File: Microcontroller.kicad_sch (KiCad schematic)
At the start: 9 parts, among them J1 GT-USB-7010ASV, SW1 CK_KMS2xxGP, U1 ESP32-S3-MINI-1

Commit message: Added power latch circuit.
Signed-off-by: James Mendel <jrm.mendel@gmail.com>
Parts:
- removed C7: 0.1u, symbol Device:C
- removed SW1: CK_KMS2xxGP, Button_Switch_SMD:SW_SPST_CK_KMS2xxGP, symbol Switch:CK_KMS2xxGP
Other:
- note removed: "Switch"

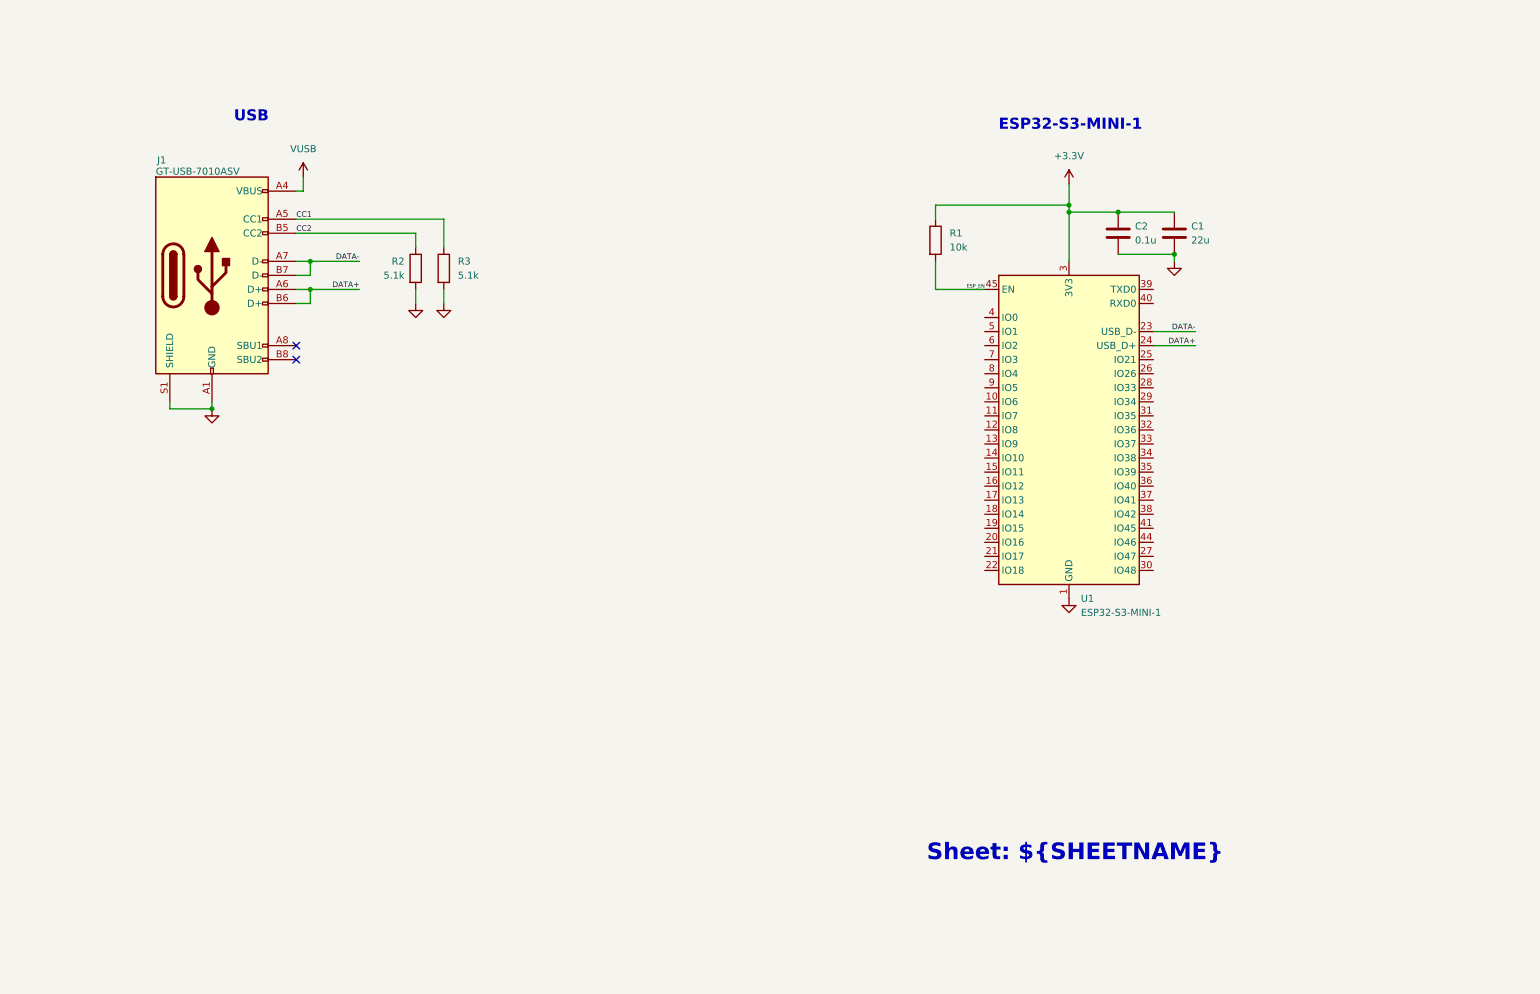
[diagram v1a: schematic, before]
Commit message: SCH and PCB updates. Added Integrated GPS and other features.
Signed-off-by: James Mendel <jrm.mendel@gmail.com>
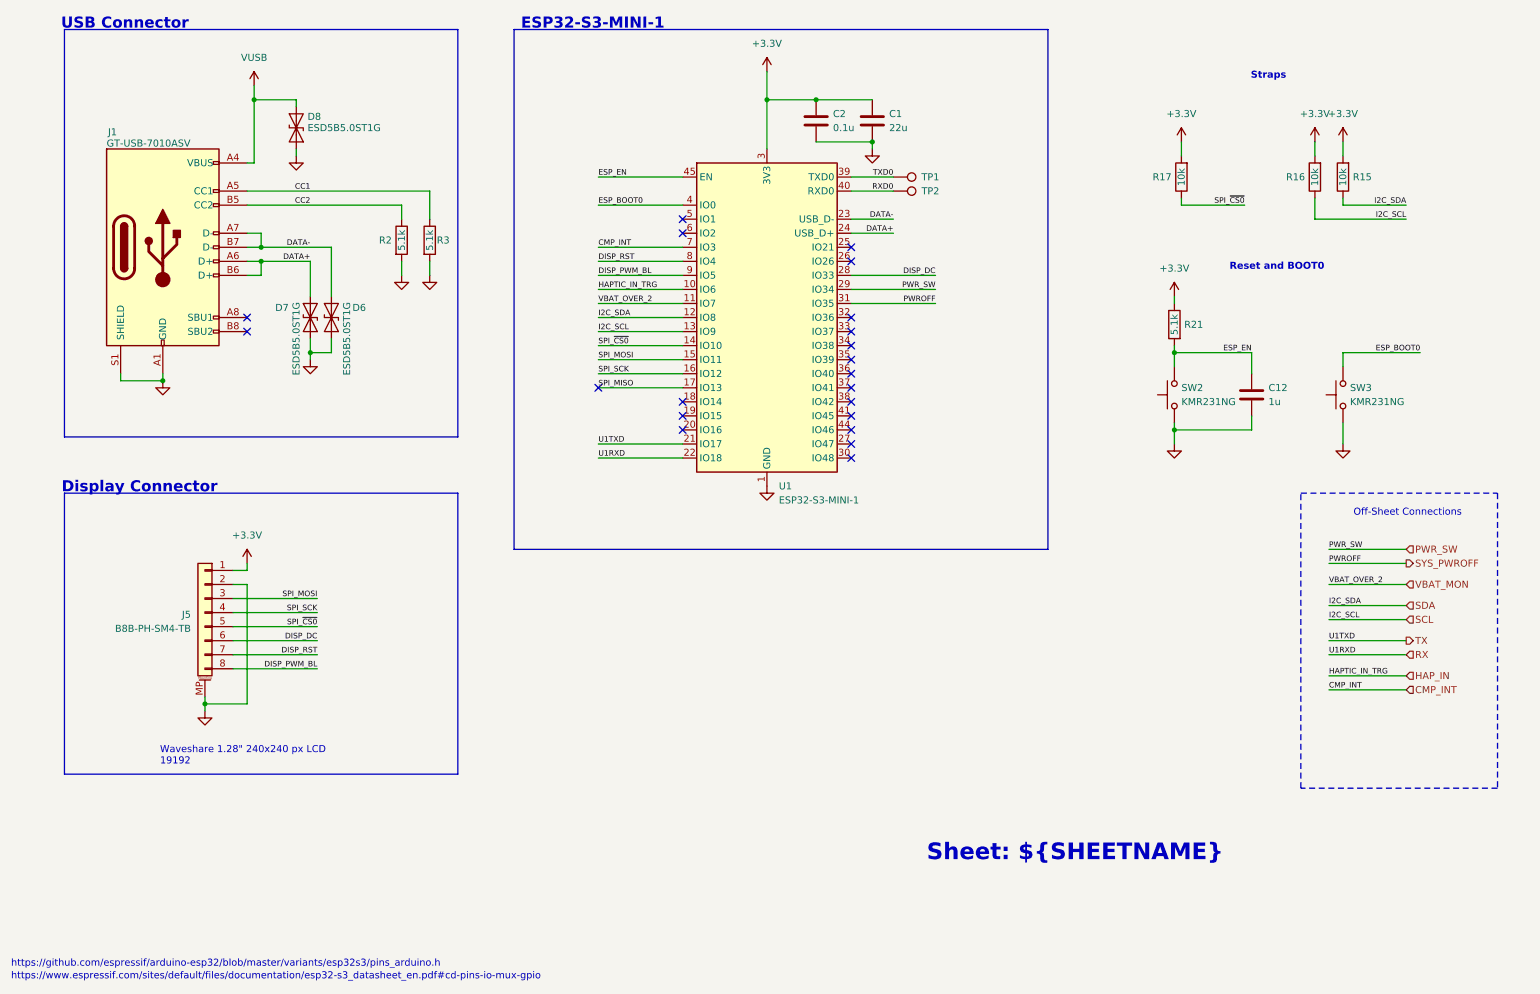
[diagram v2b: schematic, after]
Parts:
- removed R1: 10k, symbol Device:R
- added C12: 1u, Capacitor_SMD:C_0603_1608Metric, symbol Device:C
- added D6, D7, D8: ESD5B5.0ST1G, Diode_SMD:D_SOD-523, symbol Diode:ESD9B5.0ST5G
- added J5: B8B-PH-SM4-TB, Connector_JST:JST_PH_B8B-PH-SM4-TB_1x08-1MP_P2.00mm_Vertical, symbol Connector_Generic_MountingPin:Conn_01x08_MountingPin
- added R15, R16, R17: 10k, Resistor_SMD:R_0603_1608Metric, symbol Device:R
- added R21: 5.1k, Resistor_SMD:R_0603_1608Metric, symbol Device:R
- added SW2, SW3: KMR231NG, Button_Switch_SMD:SW_Push_1P1T_NO_CK_KMR2, symbol Switch:SW_Push
- added TP1: TXD0, TestPoint:TestPoint_Pad_D1.5mm, symbol Connector:TestPoint
- added TP2: RXD0, TestPoint:TestPoint_Pad_D1.5mm, symbol Connector:TestPoint
- C1, C2: footprint (none) -> Capacitor_SMD:C_0603_1608Metric
- J1: Alt1 (none) -> USB4105-GF-A; MPN (none) -> GT-USB-7010ASV
- R2, R3: footprint (none) -> Resistor_SMD:R_0603_1608Metric
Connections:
- net +3.3V: now also J5.1 (Pin_1), R15.2, R16.2, R17.2, R21.1
- net DATA+: now also D7.2 (A2)
- net DATA-: now also D6.2 (A2)
- net ESP_EN: now also C12.1, R21.2, SW2.2
- net GND: now also C12.2, D6.1 (A1), D7.1 (A1), D8.1 (A1), J5.2 (Pin_2), J5.MP (MountPin), SW2.1, SW3.1
- net VUSB: now also D8.2 (A2)
- net HAP_IN: now reaches U1.10 (IO6)
- net VBAT_MON: now reaches U1.11 (IO7)
- net SDA: now reaches U1.12 (IO8)
- net SDA: now also R15.1
- net SCL: now reaches U1.13 (IO9)
- net SCL: now also R16.1
- net SPI_~{CS0}: now reaches U1.14 (IO10)
- net SPI_~{CS0}: now also J5.5 (Pin_5), R17.1
- net SPI_MOSI: now reaches U1.15 (IO11)
- net SPI_MOSI: now also J5.3 (Pin_3)
- net SPI_SCK: now reaches U1.16 (IO12)
- net SPI_SCK: now also J5.4 (Pin_4)
- net SPI_MISO: now reaches U1.17 (IO13)
- net TX: now reaches U1.21 (IO17)
- net RX: now reaches U1.22 (IO18)
- net DISP_DC: now reaches U1.28 (IO33)
- net DISP_DC: now also J5.6 (Pin_6)
- net PWR_SW: now reaches U1.29 (IO34)
- net SYS_PWROFF: now reaches U1.31 (IO35)
- net TXD0: now reaches U1.39 (TXD0)
- net TXD0: now also TP1.1
- net ESP_BOOT0: now reaches U1.4 (IO0)
- net ESP_BOOT0: now also SW3.2
- net RXD0: now reaches U1.40 (RXD0)
- net RXD0: now also TP2.1
- net CMP_INT: now reaches U1.7 (IO3)
- net DISP_RST: now reaches U1.8 (IO4)
- net DISP_RST: now also J5.7 (Pin_7)
- net DISP_PWM_BL: now reaches U1.9 (IO5)
- net DISP_PWM_BL: now also J5.8 (Pin_8)
- no-connect marks 2 -> 21
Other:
- note added: "Display Connector"
- note added: "Off-Sheet Connections"
- note added: "Reset and BOOT0"
- note added: "Straps"
- note added: "USB Connector"
- note added: "Waveshare 1.28" 240x240 px LCD 19192"
- note added: "https://github.com/espressif/arduino-esp32/blob/master/variants/esp32s3/pins_arduino.h"
- note added: "https://www.espressif.com/sites/default/files/documentation/esp32-s3_datasheet_en.pdf#cd-pins-io-mux-gpio"
- note removed: "USB"
- moved on the sheet: C1, C2, J1, R2, R3, U1

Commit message: Updated board outline to version 004
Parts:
- removed R17: 10k, Resistor_SMD:R_0603_1608Metric, symbol Device:R
- added TP10: SPI_MOSI, M20048-1:TestPoint_Pad_D1.5mm_WITH_LABEL, symbol Connector:TestPoint
- added TP11: SPI_SCK, M20048-1:TestPoint_Pad_D1.5mm_WITH_LABEL, symbol Connector:TestPoint
- added TP12: TXD0, M20048-1:TestPoint_Pad_D1.5mm_WITH_LABEL, symbol Connector:TestPoint
- added TP13: VUSB, M20048-1:TestPoint_Pad_D1.5mm_WITH_LABEL, symbol Connector:TestPoint
- added TP7: I2C_SDA, M20048-1:TestPoint_Pad_D1.5mm_WITH_LABEL, symbol Connector:TestPoint
- added TP8: I2C_SCL, M20048-1:TestPoint_Pad_D1.5mm_WITH_LABEL, symbol Connector:TestPoint
- added TP9: SPI_CS0, M20048-1:TestPoint_Pad_D1.5mm_WITH_LABEL, symbol Connector:TestPoint
- R15, R16: value 10k -> 5.1k
- TP1, TP2: footprint TestPoint:TestPoint_Pad_D1.5mm -> M20048-1:TestPoint_Pad_D1.5mm_WITH_LABEL
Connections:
- net +3.3V: now also R15.1, R16.1; no longer R15.2, R16.2
- net CMP_INT: now also U1.33 (IO37); no longer U1.7 (IO3)
- net SCL: now also R16.2, TP8.1; no longer R16.1
- net SDA: now also R15.2, TP7.1; no longer R15.1
- net SPI_MISO: now also TP12.1
- net SPI_MOSI: now also TP10.1
- net SPI_SCK: now also TP11.1
- net SPI_~{CS0}: now also TP9.1
- net VUSB: now also TP13.1
- net CMP_~{RST}: now reaches U1.34 (IO38)
- net GPS_~{RST}: now reaches U1.35 (IO39)
- net GPS_STBY: now reaches U1.36 (IO40)
- net GPS_FIX: now reaches U1.37 (IO41)
- no-connect marks 21 -> 16
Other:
- note added: "Layout note: Place test points on bottom side"
- note added: "Note: Parasitic is 32pF D7, D6 Compatible with USB 1.1 FS (<! 75pF)"

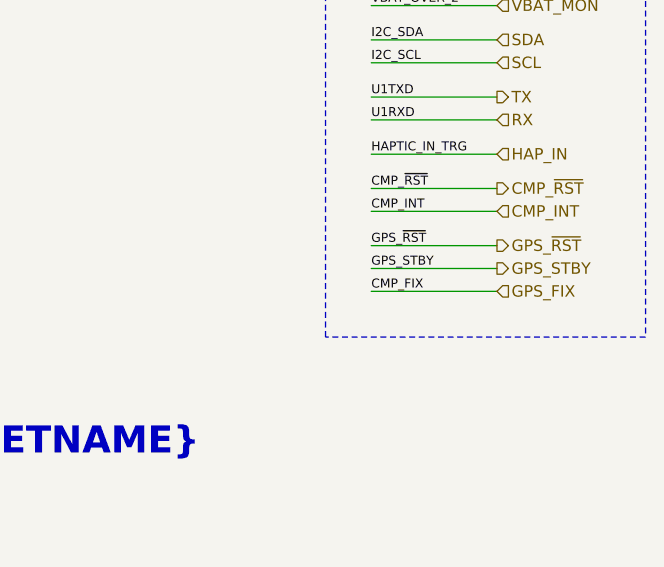
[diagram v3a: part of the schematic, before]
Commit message: Component placement for -004 board outline.
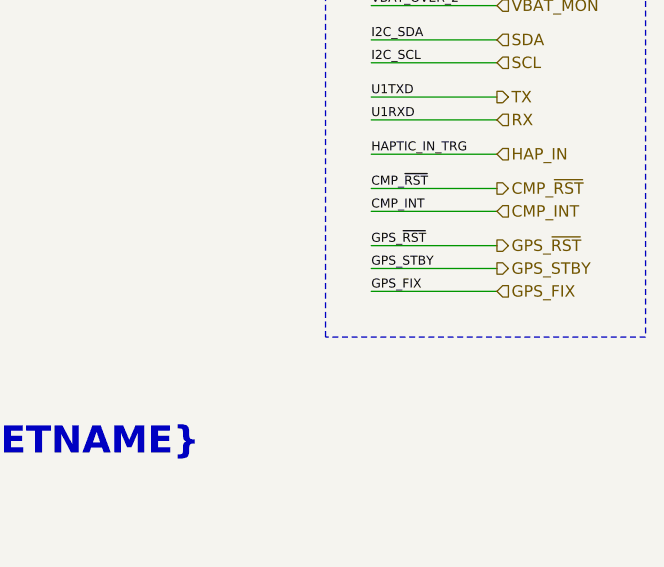
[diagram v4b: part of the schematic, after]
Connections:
- net GPS_FIX: no longer U1.37 (IO41)
- new net CMP_FIX: U1.37 (IO41)
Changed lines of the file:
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@@
 		)
 	)
-	(label "CMP_FIX"
+	(label "GPS_FIX"
 		(at 251.46 157.48 0)
 		(effects

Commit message: Lots of board layout
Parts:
- removed J5: B8B-PH-SM4-TB, Connector_JST:JST_PH_B8B-PH-SM4-TB_1x08-1MP_P2.00mm_Vertical, symbol Connector_Generic_MountingPin:Conn_01x08_MountingPin
- removed U1: ESP32-S3-MINI-1, RF_Module:ESP32-S2-MINI-1, symbol RF_Module:ESP32-S3-MINI-1
- added D10: GPIO48, Diode_SMD:D_0603_1608Metric, symbol Device:LED
- added R26: 1.5k, Resistor_SMD:R_0603_1608Metric, symbol Device:R
- added U1: ESP32-S3-MINI-1, RF_Module:ESP32-S2-MINI-1, symbol RF_Module1:ESP32-S3-MINI-1
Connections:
- net +3.3V: now also U1.3 (3V3)
- net CMP_INT: now also U1.33 (SPIDQS/GPIO37/FSPIQ/SUBSPIQ)
- net CMP_~{RST}: now also U1.34 (GPIO38/FSPIWP/SUBSPIWP)
- net DATA+: now also U1.24 (USB_D+)
- net DATA-: now also U1.23 (USB_D-)
- net DISP_DC: now also U1.28 (SPIIO4/GPIO33/FSPIHD/SUBSPIHD)
- net DISP_PWM_BL: now also U1.9 (RTC_GPIO5/GPIO5/TOUCH5/ADC1_CH4)
- net ESP_BOOT0: now also U1.4 (RTC_GPIO0/GPIO0)
- net ESP_EN: now also U1.45 (EN)
- net GND: now also D10.1 (K), U1.1 (GND), U1.2 (GND), U1.42 (GND), U1.43 (GND), U1.46 (GND), U1.47 (GND), U1.48 (GND), U1.49 (GND), U1.50 (GND), U1.51 (GND), U1.52 (GND), U1.53 (GND), U1.54 (GND), U1.55 (GND), U1.56 (GND), U1.57 (GND), U1.58 (GND), U1.59 (GND), U1.60 (GND), U1.61 (GND), U1.62 (GND), U1.63 (GND), U1.64 (GND), U1.65 (GND)
- net GPS_FIX: now also U1.37 (MTDI/GPIO41/CLK_OUT1)
- net GPS_STBY: now also U1.36 (MTDO/GPIO40/CLK_OUT2)
- net GPS_~{RST}: now also U1.35 (MTCK/GPIO39/CLK_OUT3/SUBSPICS1)
- net HAP_IN: now also U1.38 (MTMS/GPIO42)
- net PWR_SW: now also U1.29 (SPIIO5/GPIO34/FSPICS0/SUBSPICS0)
- net RX: now also U1.22 (RTC_GPIO18/GPIO18/U1RXD/ADC2_CH7/CLK_OUT3)
- net SCL: now also U1.13 (RTC_GPIO9/GPIO9/TOUCH9/ADC1_CH8/FSPIHD/SUBSPIHD)
- net SDA: now also U1.12 (RTC_GPIO7/GPIO7/TOUCH7/ADC1_CH6)
- net SPI_MISO: now also U1.17 (RTC_GPIO13/GPIO13/TOUCH13/ADC2_CH2/FSPIQ/FSPIIO7/SUBSPIQ)
- net SPI_MOSI: now also U1.15 (RTC_GPIO11/GPIO11/TOUCH11/ADC2_CH0/FSPID/FSPIIO5/SUBSPID)
- net SPI_SCK: now also U1.16 (RTC_GPIO12/GPIO12/TOUCH12/ADC2_CH1/FSPICLK/FSPIIO6/SUBSPICLK)
- net SYS_PWROFF: now also U1.31 (SPIIO6/GPIO35/FSPID/SUBSPID)
- net TX: now also U1.21 (RTC_GPIO17/GPIO17/U1TXD/ADC2_CH6)
- net VBAT_MON: now also U1.5 (RTC_GPIO1/GPIO1/TOUCH1/ADC1_CH0)
- net RXD0 renamed U0RXD
- net U0RXD: now also U1.40 (U0RXD/GPIO44/CLK_OUT2)
- net SPI_~{CS0} renamed SPI_~{CS0_DISP}
- net SPI_~{CS0_DISP}: now also U1.14 (RTC_GPIO10/GPIO10/TOUCH10/ADC1_CH9/FSPICS0/FSPIIO4/SUBSPICS0)
- net TXD0 renamed U0TXD
- net U0TXD: now also U1.39 (U0TXD/GPIO43/CLK_OUT1)
- new net: D10.2 (A), R26.2
- new net DISP_~{RST}: U1.8 (RTC_GPIO4/GPIO4/TOUCH4/ADC1_CH3)
- new net LED_GPIO48: R26.1, U1.30 (SPICLK_N_DIFF/GPIO48/SUBSPICLK_N_DIFF)
- no-connect marks 16 -> 15
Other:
- note added: "LED for Debug"
- note added: "Reset and Bootloader switches"
- note added: "USB-C Connector"
- note removed: "Display Connector"
- note removed: "Reset and BOOT0"
- note removed: "Straps"
- note removed: "USB Connector"
- note removed: "Waveshare 1.28" 240x240 px LCD 19192"
- moved on the sheet: C1, C12, C2, D6, D7, D8, J1, R15, R16, R2, R21, R3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

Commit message: More layout and sch updates, ready for final review.
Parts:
- D6, D7, D8: value ESD5B5.0ST1G -> DESD5V0U1BB-7; MPN (none) -> DESD5V0U1BB-7
- SW2, SW3: MPN (none) -> KMR231NG
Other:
- note removed: "Note: Parasitic is 32pF D7, D6 Compatible with USB 1.1 FS (<! 75pF)"
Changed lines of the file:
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@@
 	(title_block
 		(title "${TITLE}")
-		(date "2025-03-23")
+		(date "2025-04-05")
 		(rev "${REVISION}")
 		(company "J. MENDEL")
@@
 		)
 	)
-	(text "Note: Parasitic is 32pF\nD7, D6 Compatible with\nUSB 1.1 FS (<! 75pF)"
-		(exclude_from_sim no)
-		(at 237.49 92.964 0)
-		(effects
-			(font
-				(size 1 1)
-				(color 132 0 132 1)
-			)
-			(justify right)
-		)
-	)
 	(text_box "Sheet: ${SHEETNAME}"
 		(exclude_from_sim no)
@@
 			)
 		)
+		(property "MPN" "KMR231NG"
+			(at 35.56 165.1 0)
+			(effects
+				(font
+					(size 1.27 1.27)
+				)
+				(hide yes)
+			)
+		)
 		(pin "2"
 		)
@@
 			)
 		)
+		(property "MPN" "KMR231NG"
+			(at 67.31 165.1 0)
+			(effects
+				(font
+					(size 1.27 1.27)
+				)
+				(hide yes)
+			)
+		)
 		(pin "2"
 		)
@@
 			)
 		)
-		(property "Value" "ESD5B5.0ST1G"
+		(property "Value" "DESD5V0U1BB-7"
 			(at 232.41 74.676 0)
 			(effects
@@
 			)
 		)
-		(property "Datasheet" "https://www.onsemi.com/pdf/datasheet/esd5b5.0st1-d.pdf"
+		(property "Datasheet" "https://www.diodes.com/assets/Datasheets/DESD5V0U1BB.pdf"
 			(at 229.87 77.47 0)
 			(effects
@@
 			)
 		)
+		(property "MPN" "DESD5V0U1BB-7"
+			(at 229.87 77.47 0)
+			(effects
+				(font
+					(size 1.27 1.27)
+				)
+				(hide yes)
+			)
+		)
 		(pin "1"
 		)
@@
 			)
 		)
-		(property "Value" "ESD5B5.0ST1G"
+		(property "Value" "DESD5V0U1BB-7"
 			(at 230.378 43.18 90)
 			(effects
@@
 			)
 		)
-		(property "Datasheet" "https://www.onsemi.com/pdf/datasheet/esd5b5.0st1-d.pdf"
+		(property "Datasheet" "https://www.diodes.com/assets/Datasheets/DESD5V0U1BB.pdf"
 			(at 232.41 43.18 0)
 			(effects
@@
 			)
 		)
+		(property "MPN" "DESD5V0U1BB-7"
+			(at 232.41 43.18 0)
+			(effects
+				(font
+					(size 1.27 1.27)
+				)
+				(hide yes)
+			)
+		)
 		(pin "1"
 		)
@@
 			)
 		)
-		(property "Datasheet" "~"
+		(property "Datasheet" "https://mm.digikey.com/Volume0/opasdata/d220001/medias/docus/858/LTST-C190GKT.pdf"
 			(at 208.28 115.57 0)
 			(effects
@@
 			)
 		)
-		(property "Value" "ESD5B5.0ST1G"
+		(property "Value" "DESD5V0U1BB-7"
 			(at 223.266 74.676 0)
 			(effects
@@
 			)
 		)
-		(property "Datasheet" "https://www.onsemi.com/pdf/datasheet/esd5b5.0st1-d.pdf"
+		(property "Datasheet" "https://www.diodes.com/assets/Datasheets/DESD5V0U1BB.pdf"
 			(at 226.06 77.47 0)
 			(effects
@@
 			(at 226.06 77.47 0)
 			(effects
+				(font
+					(size 1.27 1.27)
+				)
+				(hide yes)
+			)
+		)
+		(property "MPN" "DESD5V0U1BB-7"
+			(at 226.06 77.47 0)
+			(effects
